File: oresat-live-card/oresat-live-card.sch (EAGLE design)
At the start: 281 parts, among them J1 ORESAT-DEBUG-CONNECTOR-CARD, J100 DM3BT-DSF-PEJS, J102 FTSH-105-XX-X-DV-K, J2 SM06B-SRSS-TB(LF)(SN), J4 TFM-120-01-L-D-RA, Q1 MMBT2907, Q2 PMV45EN, Q3 DMP2240UDM, Q4 PMV45EN, Q5 MOSFET-PCH-SOT23-6, Q6 MOSFET-PCH-SOT23-6, U1 RCLAMP0504FB, U10 TLVH431, U11 TCAN330, U12 MIC842LYC5, U13 MIC842LYC5, U14 MAX4211FETE, U15 TPS62112, U16 MAX7310ATE, U17 25AAXX, U18 RCLAMP0504FB, U2 TPS2051CDBVR, U3 THGBMJG7C2LBAU8, U4 SN74LVC1G07DCK, U7 OSD3358-512M-BSM, Y1 24MHz, Y2 ABS07-32.768KHZ-T

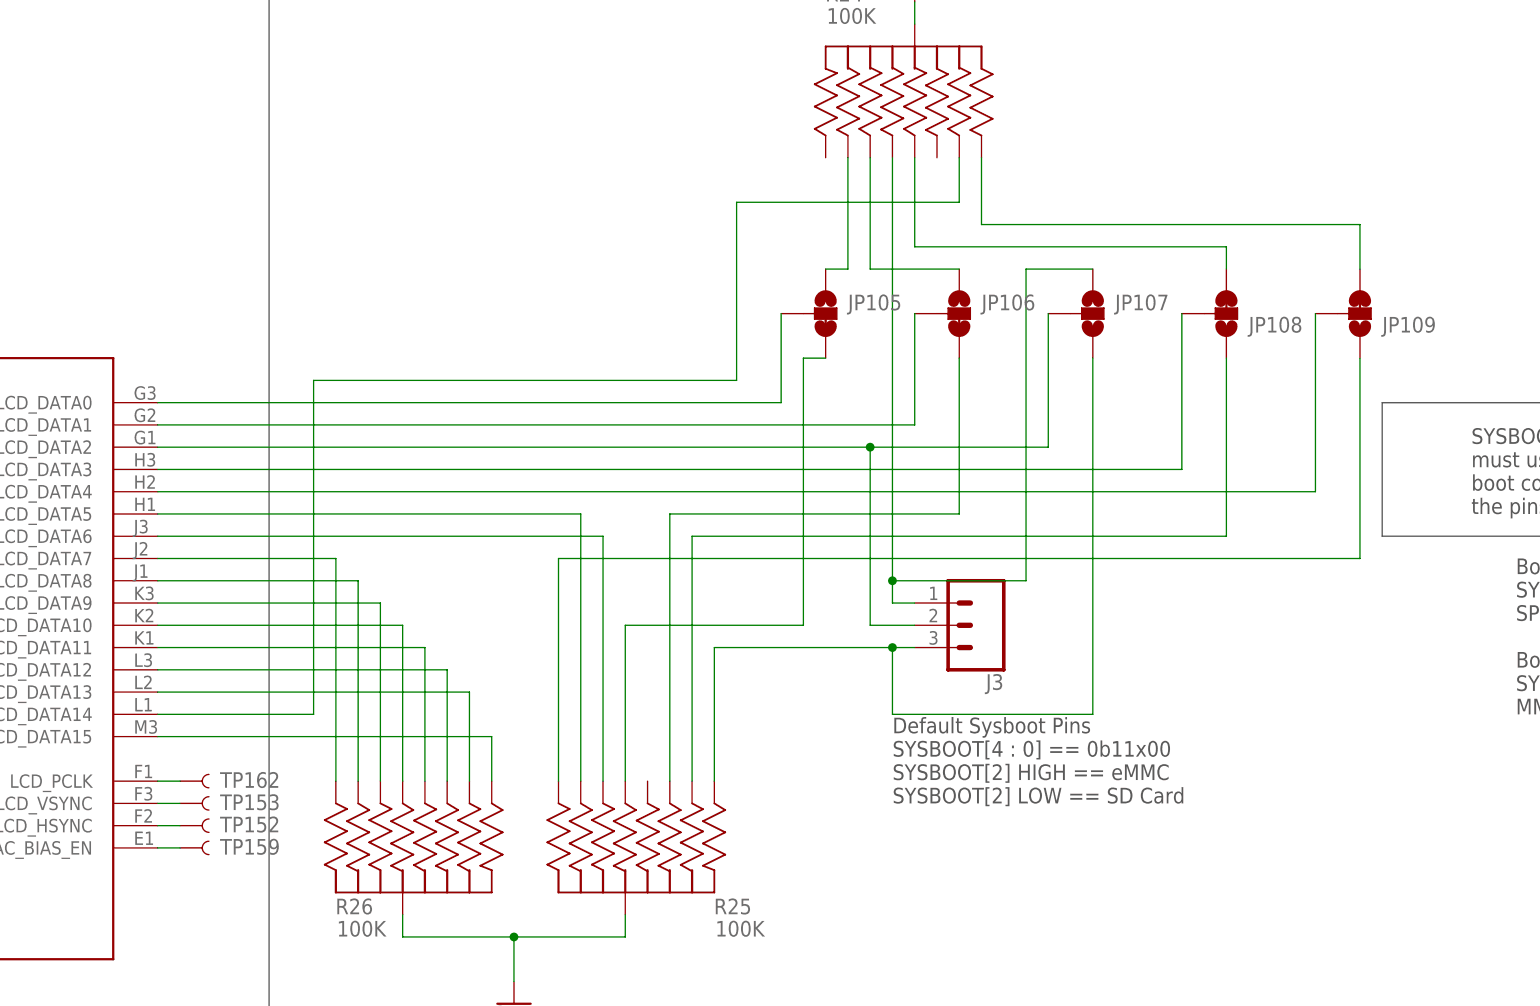
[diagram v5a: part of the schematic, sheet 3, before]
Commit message: routed boot jumpers
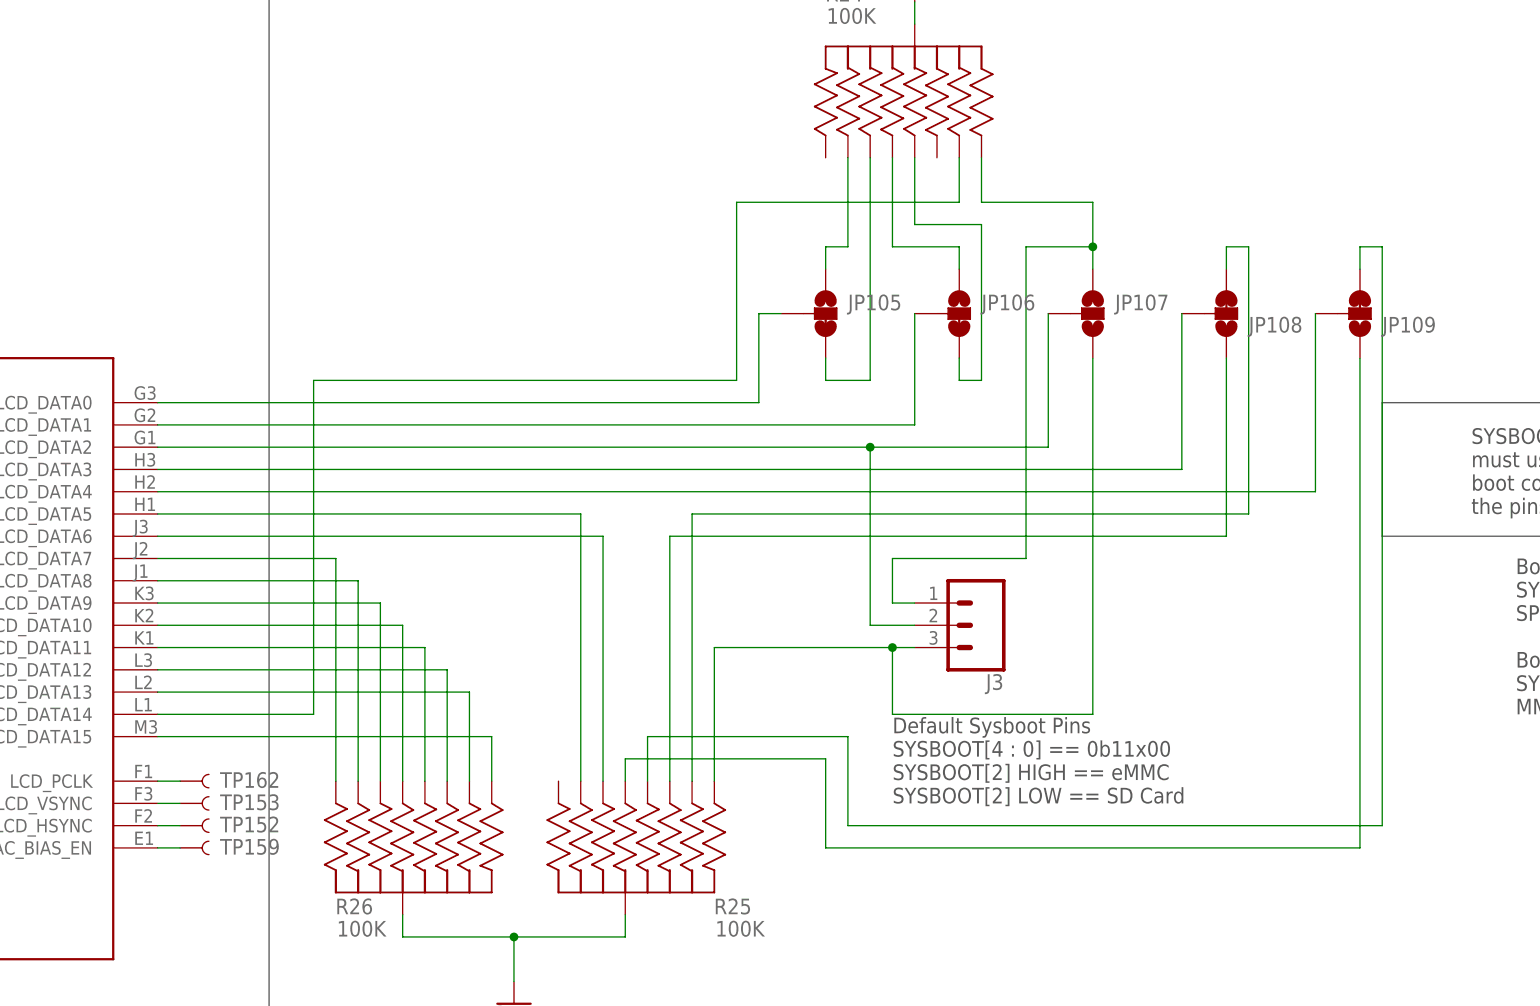
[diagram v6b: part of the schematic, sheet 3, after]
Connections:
- removed net N$630: JP109.1, R25.66
- removed net N$632: JP108.1, R25.99
- removed net N$633: JP106.3, R25.22
- removed net N$634: JP105.3, R25.33
- new net N$105: JP106.1, R24.88
- new net N$118: JP109.3, R25.88
- new net N$119: JP109.1, R25.33
- new net N$24: JP105.3, R24.22
- net N$106: now also JP106.3, R24.33; no longer JP106.1, R24.22
- net N$107: now also R25.99; no longer R24.33
- net N$108: now also JP108.1, R25.22; no longer JP109.3, R24.66
- net N$109: now also R24.66; no longer R24.88

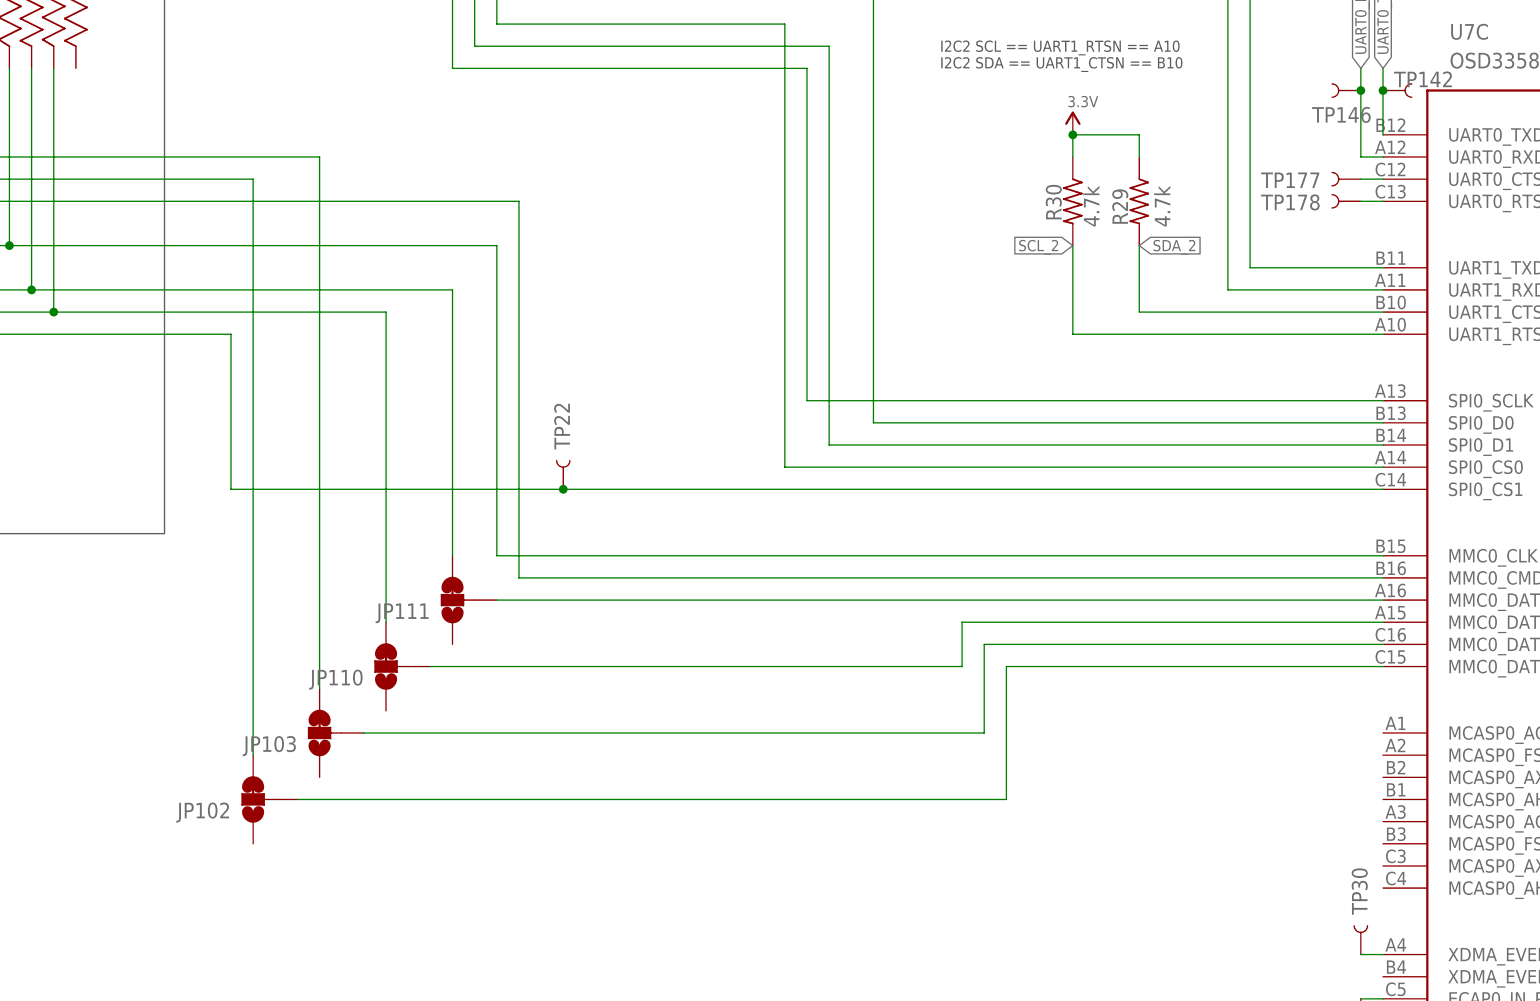
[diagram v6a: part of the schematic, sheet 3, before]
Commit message: Removed unused jumpers left over from star tracker
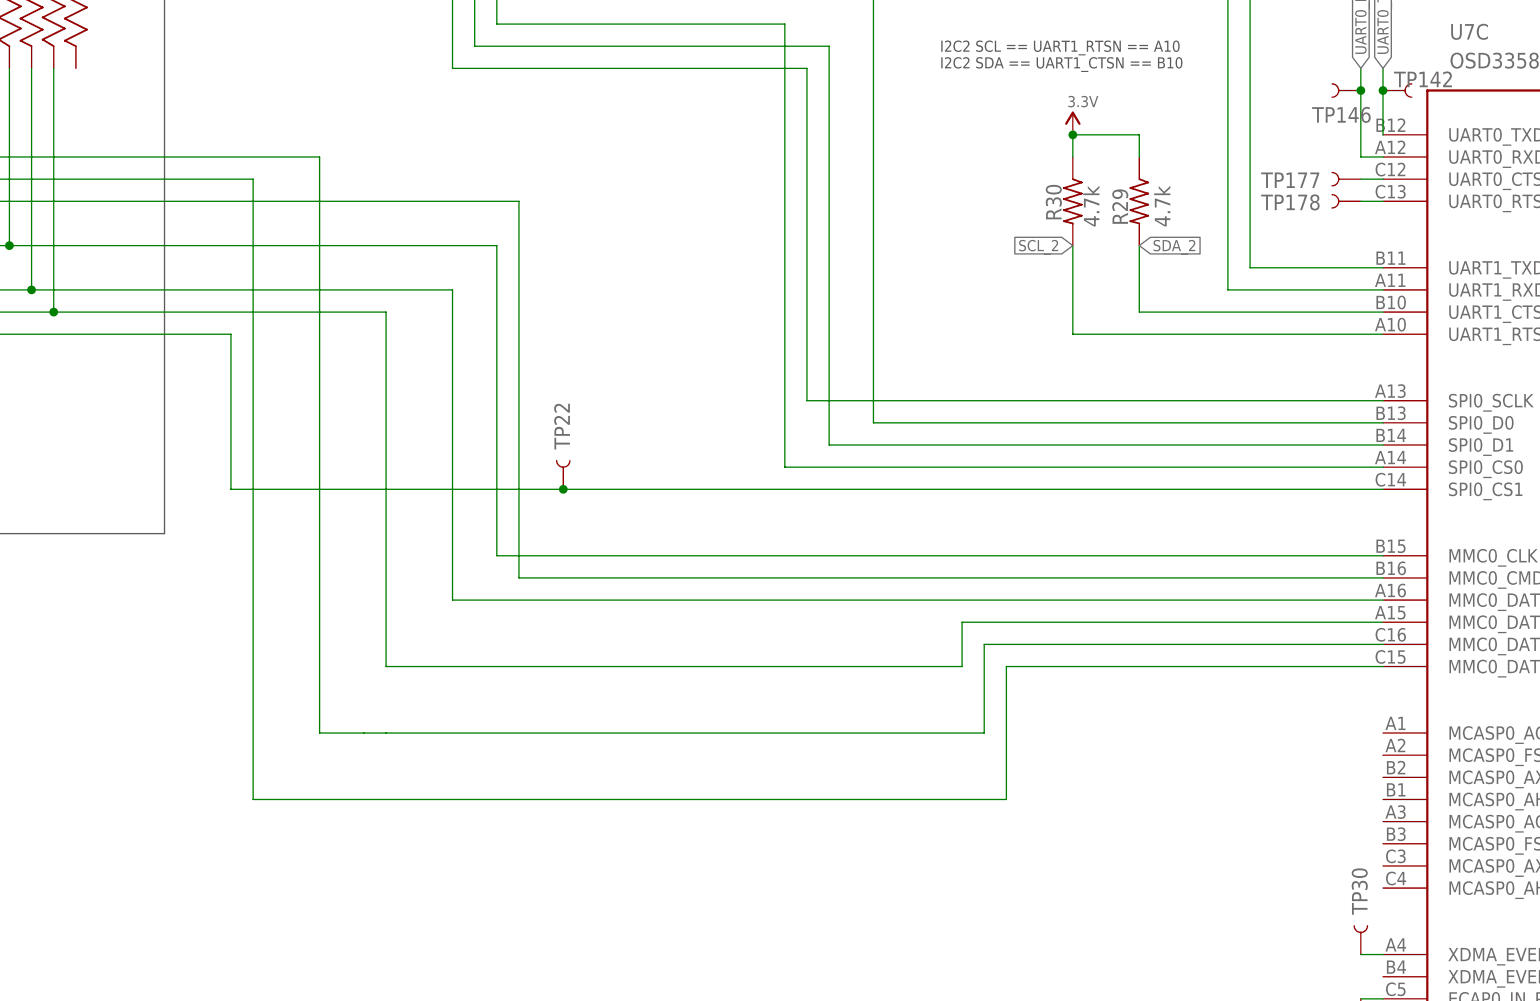
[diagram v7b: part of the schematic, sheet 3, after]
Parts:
- removed JP102, JP103, JP110, JP111: JUMPER-SMT_3_1-NC_TRACE_SILK, SparkFun-Jumpers:JUMPER-SMT_3_1-NC_TRACE_SILK
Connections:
- removed net N$15: JP111.2, U7C.MMC0_DAT0
- removed net N$16: JP110.2, U7C.MMC0_DAT1
- removed net N$17: JP103.2, U7C.MMC0_DAT2
- removed net N$18: JP102.2, U7C.MMC0_DAT3
- net N$4: now also U7C.MMC0_DAT2; no longer JP103.3
- net N$5: now also U7C.MMC0_DAT3; no longer JP102.3
- net N$8: now also U7C.MMC0_DAT0; no longer JP111.3
- net N$9: now also U7C.MMC0_DAT1; no longer JP110.3
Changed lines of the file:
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@@
 <part name="C13" library="oresat-rcl" deviceset="C-EU" device="C1210" value="22uF"/>
 <part name="GND68" library="SparkFun-PowerSymbols" deviceset="GND" device=""/>
-<part name="JP111" library="SparkFun-Jumpers" deviceset="JUMPER-SMT_3_1-NC_TRACE" device="_SILK"/>
-<part name="JP110" library="SparkFun-Jumpers" deviceset="JUMPER-SMT_3_1-NC_TRACE" device="_SILK"/>
-<part name="JP103" library="SparkFun-Jumpers" deviceset="JUMPER-SMT_3_1-NC_TRACE" device="_SILK"/>
-<part name="JP102" library="SparkFun-Jumpers" deviceset="JUMPER-SMT_3_1-NC_TRACE" device="_SILK"/>
 <part name="R30" library="oresat-rcl" deviceset="R-US_" device="0603-A" value="4.7k"/>
 <part name="R29" library="oresat-rcl" deviceset="R-US_" device="0603-A" value="4.7k"/>
@@
 <attribute name="NAME" x="248.412" y="514.858" size="1.778" layer="95" font="vector"/>
 </instance>
-<instance part="JP111" gate="G$1" x="182.88" y="353.06" smashed="yes" rot="R180">
-<attribute name="NAME" x="180.34" y="352.679" size="1.778" layer="95" font="vector" rot="R180"/>
-</instance>
-<instance part="JP110" gate="G$1" x="175.26" y="345.44" smashed="yes" rot="R180">
-<attribute name="NAME" x="172.72" y="345.059" size="1.778" layer="95" font="vector" rot="R180"/>
-</instance>
-<instance part="JP103" gate="G$1" x="167.64" y="337.82" smashed="yes" rot="R180">
-<attribute name="NAME" x="165.1" y="337.439" size="1.778" layer="95" font="vector" rot="R180"/>
-</instance>
-<instance part="JP102" gate="G$1" x="160.02" y="330.2" smashed="yes" rot="R180">
-<attribute name="NAME" x="157.48" y="329.819" size="1.778" layer="95" font="vector" rot="R180"/>
-</instance>
 <instance part="R30" gate="R" x="254" y="398.78" smashed="yes" rot="R270">
 <attribute name="NAME" x="250.9266" y="400.812" size="1.778" layer="95" rot="R270"/>
@@
 <segment>
 <pinref part="J100" gate="G$1" pin="DAT2"/>
-<pinref part="JP103" gate="G$1" pin="3"/>
-<wire x1="167.64" y1="342.9" x2="167.64" y2="403.86" width="0.1524" layer="91"/>
+<wire x1="167.64" y1="337.82" x2="167.64" y2="403.86" width="0.1524" layer="91"/>
 <wire x1="167.64" y1="403.86" x2="121.92" y2="403.86" width="0.1524" layer="91"/>
 <pinref part="R8" gate="A" pin="11"/>
@@
 <wire x1="121.92" y1="414.02" x2="121.92" y2="403.86" width="0.1524" layer="91"/>
 <junction x="121.92" y="403.86"/>
+<pinref part="U7" gate="C" pin="MMC0_DAT2"/>
+<wire x1="289.56" y1="347.98" x2="243.84" y2="347.98" width="0.1524" layer="91"/>
+<wire x1="243.84" y1="347.98" x2="243.84" y2="337.82" width="0.1524" layer="91"/>
+<wire x1="243.84" y1="337.82" x2="175.26" y2="337.82" width="0.1524" layer="91"/>
+<wire x1="175.26" y1="337.82" x2="172.72" y2="337.82" width="0.1524" layer="91"/>
+<wire x1="167.64" y1="337.82" x2="172.72" y2="337.82" width="0.1524" layer="91"/>
 </segment>
 </net>
@@
 <segment>
 <pinref part="J100" gate="G$1" pin="DAT3/CS"/>
-<pinref part="JP102" gate="G$1" pin="3"/>
-<wire x1="160.02" y1="335.28" x2="160.02" y2="401.32" width="0.1524" layer="91"/>
+<wire x1="160.02" y1="330.2" x2="160.02" y2="401.32" width="0.1524" layer="91"/>
 <wire x1="160.02" y1="401.32" x2="127" y2="401.32" width="0.1524" layer="91"/>
 <pinref part="R8" gate="A" pin="22"/>
@@
 <wire x1="127" y1="414.02" x2="127" y2="401.32" width="0.1524" layer="91"/>
 <junction x="127" y="401.32"/>
+<pinref part="U7" gate="C" pin="MMC0_DAT3"/>
+<wire x1="289.56" y1="345.44" x2="246.38" y2="345.44" width="0.1524" layer="91"/>
+<wire x1="246.38" y1="345.44" x2="246.38" y2="330.2" width="0.1524" layer="91"/>
+<wire x1="246.38" y1="330.2" x2="160.02" y2="330.2" width="0.1524" layer="91"/>
 </segment>
 </net>
@@
 <segment>
 <pinref part="J100" gate="G$1" pin="DAT0/DO"/>
-<pinref part="JP111" gate="G$1" pin="3"/>
 <wire x1="106.68" y1="388.62" x2="134.62" y2="388.62" width="0.1524" layer="91"/>
 <wire x1="134.62" y1="388.62" x2="182.88" y2="388.62" width="0.1524" layer="91"/>
-<wire x1="182.88" y1="388.62" x2="182.88" y2="358.14" width="0.1524" layer="91"/>
+<wire x1="182.88" y1="388.62" x2="182.88" y2="353.06" width="0.1524" layer="91"/>
 <pinref part="R8" gate="A" pin="77"/>
 <wire x1="134.62" y1="414.02" x2="134.62" y2="388.62" width="0.1524" layer="91"/>
 <junction x="134.62" y="388.62"/>
+<pinref part="U7" gate="C" pin="MMC0_DAT0"/>
+<wire x1="289.56" y1="353.06" x2="182.88" y2="353.06" width="0.1524" layer="91"/>
 </segment>
 </net>
@@
 <segment>
 <pinref part="J100" gate="G$1" pin="DAT1"/>
-<pinref part="JP110" gate="G$1" pin="3"/>
-<wire x1="175.26" y1="350.52" x2="175.26" y2="386.08" width="0.1524" layer="91"/>
+<wire x1="175.26" y1="345.44" x2="175.26" y2="386.08" width="0.1524" layer="91"/>
 <wire x1="175.26" y1="386.08" x2="137.16" y2="386.08" width="0.1524" layer="91"/>
 <pinref part="R8" gate="A" pin="44"/>
@@
 <wire x1="137.16" y1="414.02" x2="137.16" y2="386.08" width="0.1524" layer="91"/>
 <junction x="137.16" y="386.08"/>
+<pinref part="U7" gate="C" pin="MMC0_DAT1"/>
+<wire x1="289.56" y1="350.52" x2="241.3" y2="350.52" width="0.1524" layer="91"/>
+<wire x1="241.3" y1="350.52" x2="241.3" y2="345.44" width="0.1524" layer="91"/>
+<wire x1="241.3" y1="345.44" x2="175.26" y2="345.44" width="0.1524" layer="91"/>
 </segment>
 </net>
@@
 </segment>
 </net>
-<net name="N$15" class="0">
-<segment>
-<pinref part="U7" gate="C" pin="MMC0_DAT0"/>
-<pinref part="JP111" gate="G$1" pin="2"/>
-<wire x1="289.56" y1="353.06" x2="187.96" y2="353.06" width="0.1524" layer="91"/>
-</segment>
-</net>
-<net name="N$16" class="0">
-<segment>
-<pinref part="U7" gate="C" pin="MMC0_DAT1"/>
-<wire x1="289.56" y1="350.52" x2="241.3" y2="350.52" width="0.1524" layer="91"/>
-<pinref part="JP110" gate="G$1" pin="2"/>
-<wire x1="241.3" y1="350.52" x2="241.3" y2="345.44" width="0.1524" layer="91"/>
-<wire x1="241.3" y1="345.44" x2="180.34" y2="345.44" width="0.1524" layer="91"/>
-</segment>
-</net>
-<net name="N$17" class="0">
-<segment>
-<pinref part="U7" gate="C" pin="MMC0_DAT2"/>
-<wire x1="289.56" y1="347.98" x2="243.84" y2="347.98" width="0.1524" layer="91"/>
-<pinref part="JP103" gate="G$1" pin="2"/>
-<wire x1="243.84" y1="347.98" x2="243.84" y2="337.82" width="0.1524" layer="91"/>
-<wire x1="243.84" y1="337.82" x2="172.72" y2="337.82" width="0.1524" layer="91"/>
-</segment>
-</net>
-<net name="N$18" class="0">
-<segment>
-<pinref part="U7" gate="C" pin="MMC0_DAT3"/>
-<wire x1="289.56" y1="345.44" x2="246.38" y2="345.44" width="0.1524" layer="91"/>
-<pinref part="JP102" gate="G$1" pin="2"/>
-<wire x1="246.38" y1="345.44" x2="246.38" y2="330.2" width="0.1524" layer="91"/>
-<wire x1="246.38" y1="330.2" x2="165.1" y2="330.2" width="0.1524" layer="91"/>
-</segment>
-</net>
